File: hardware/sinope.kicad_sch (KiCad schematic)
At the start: 31 parts, among them SW1 RESET, U1 Z80CTC, U10 74LS74, U2 Z80SIO, U3 Z80PIO, U4 Z80CPU, U5 74LS138, U6 65256, U7 27256, U8 74LS04, U9 74LS32, Y1 6.5Mhz

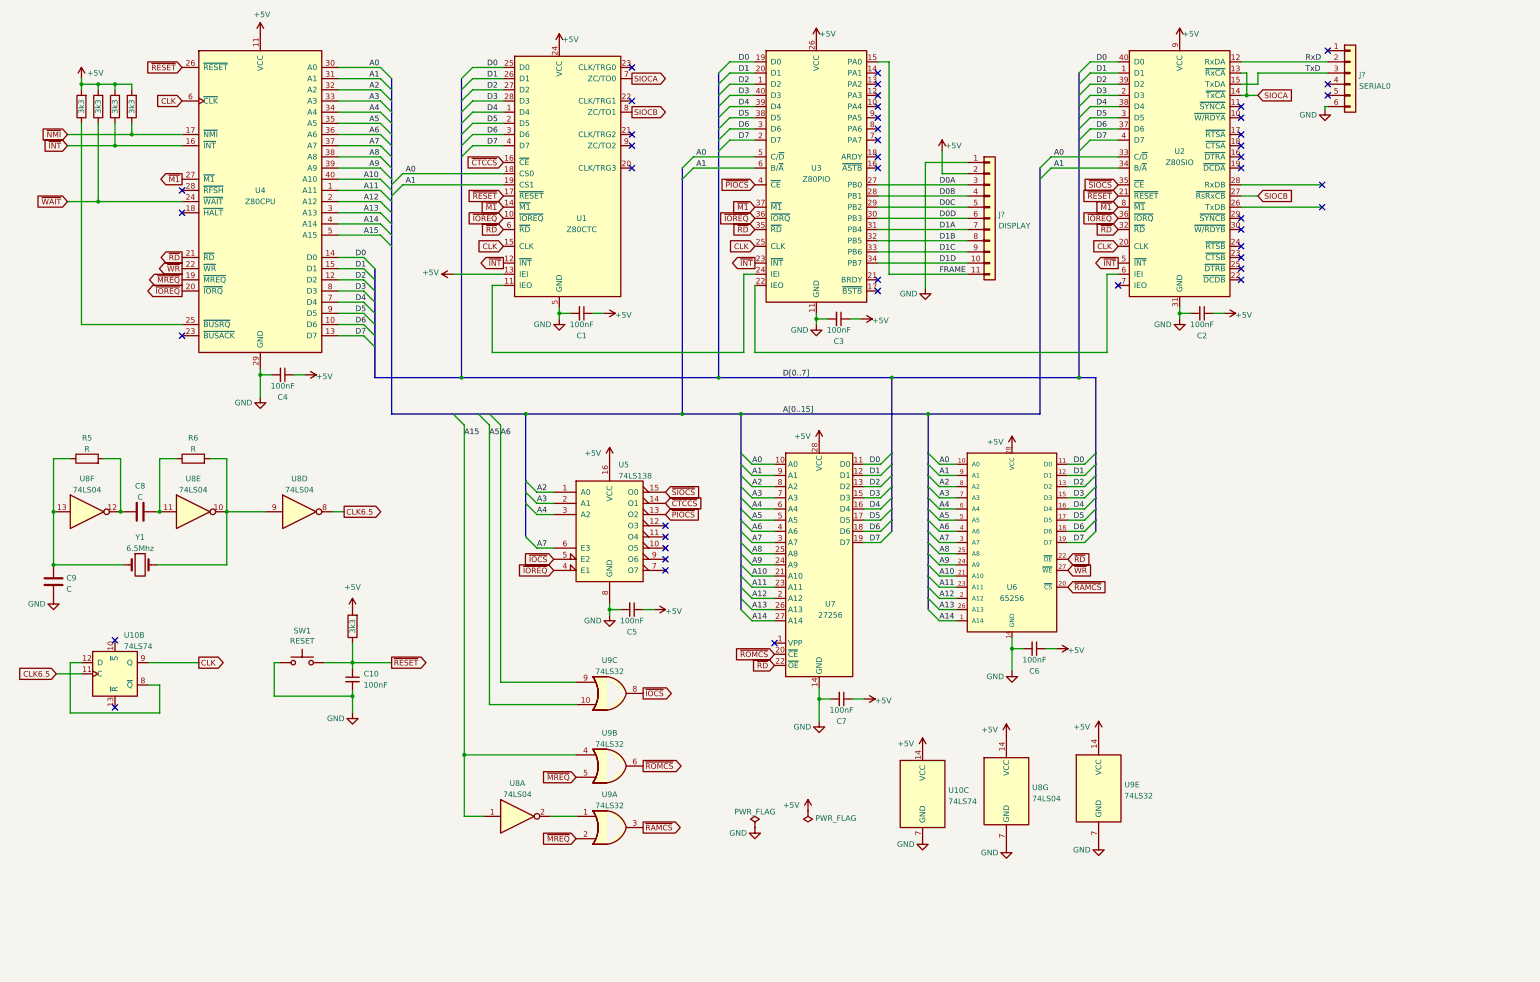
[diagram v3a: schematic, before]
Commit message: Encoder port, status led, reset tweaks, PIO reset
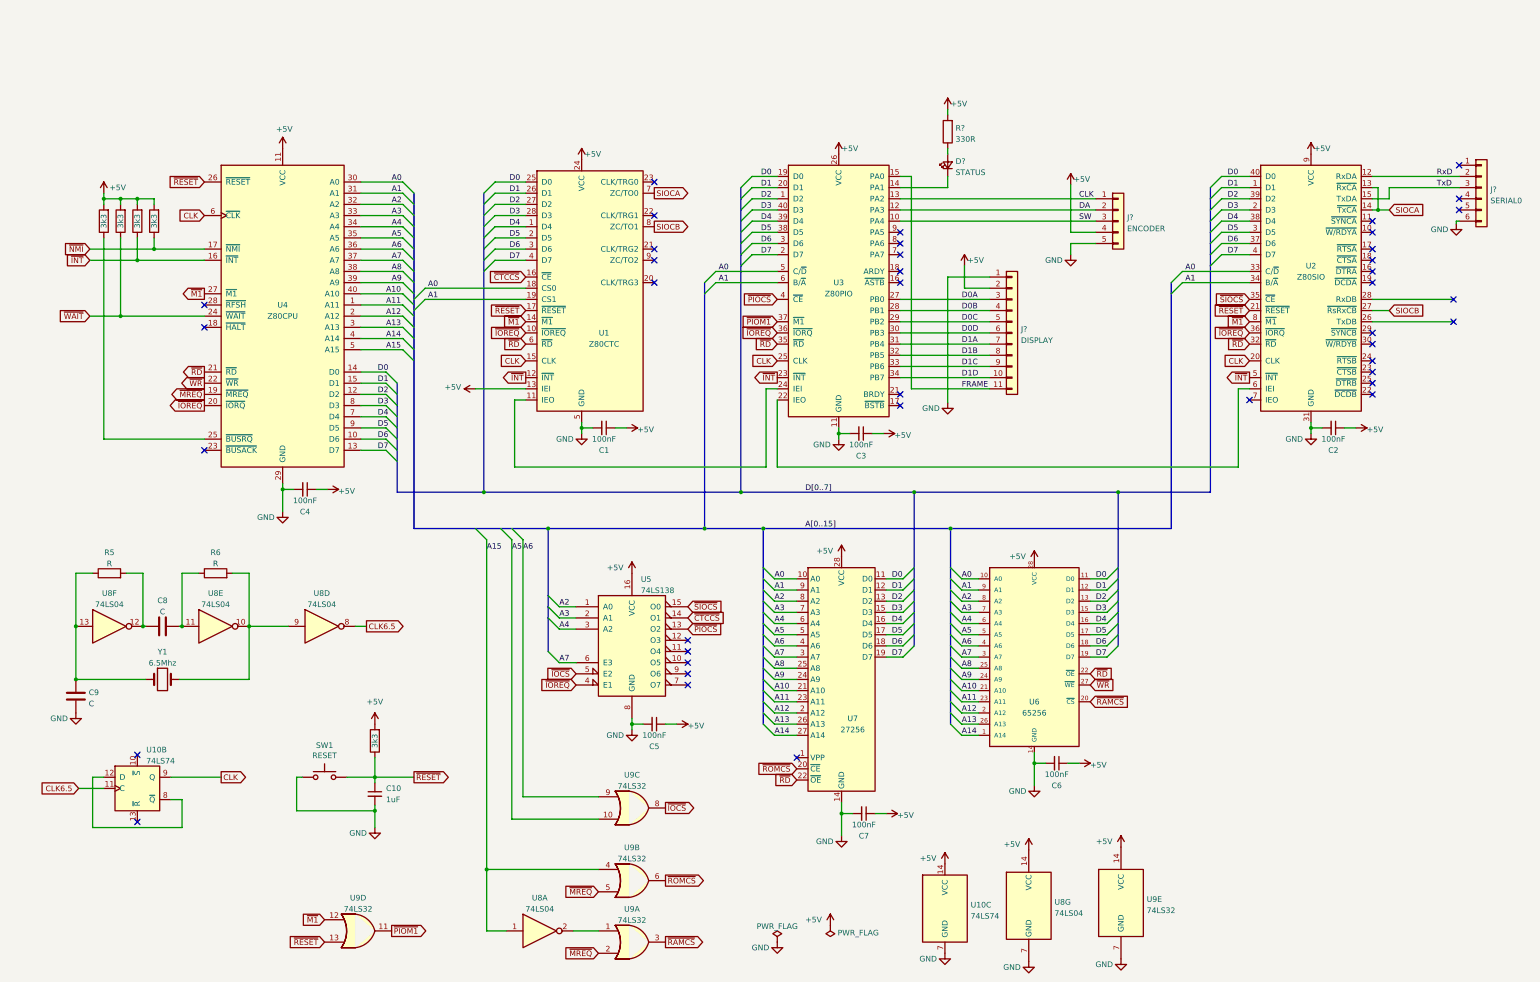
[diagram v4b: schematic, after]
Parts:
- added D?: STATUS, symbol Device:LED_Small
- added J?: ENCODER, symbol Connector_Generic:Conn_01x05
- added R?: 330R, symbol Device:R
- added unit 4 of U9
- C10: value 100nF -> 1uF
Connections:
- net +5V: now also J?.4 (Pin_4), R?.2
- net CLK: now also U3.13 (PA2), J?.1 (Pin_1)
- net GND: now also J?.5 (Pin_5)
- net ~{M1}: now also U9.12; no longer U3.37 (~{M1})
- net ~{RESET}: now also U9.13
- net SW: now reaches U3.10 (PA4)
- net SW: now also J?.3 (Pin_3)
- net DA: now reaches U3.12 (PA3)
- net DA: now also J?.2 (Pin_2)
- net at U3.14 (PA1): now also D?.1 (K)
- new net: D?.2 (A), R?.1
- new net ~{PIOM1}: U3.37 (~{M1}), U9.11
- no-connect marks 45 -> 41
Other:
- moved on the sheet: C1, C10, C2, C3, C4, C5, C6, C7, C8, C9, J?, R5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
